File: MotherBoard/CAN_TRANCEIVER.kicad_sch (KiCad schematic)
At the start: 39 parts, among them U601 PTCAN1462DRQ1, U602 PTCAN1462DRQ1

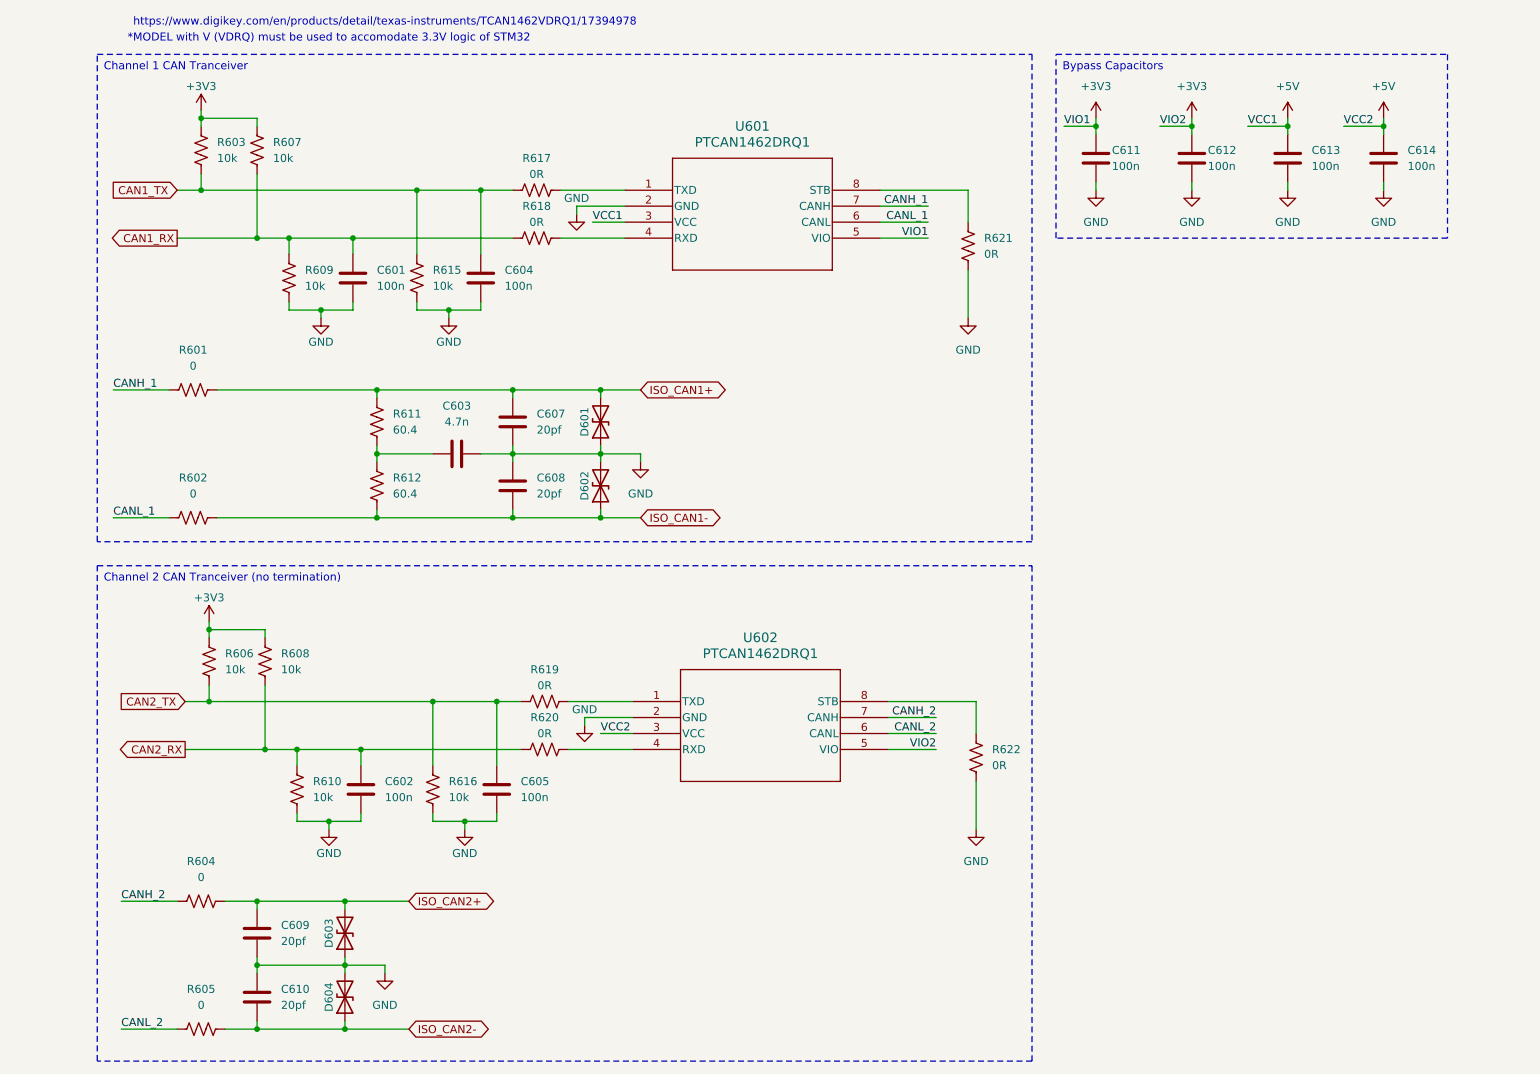
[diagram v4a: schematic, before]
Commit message: Added more 3D models
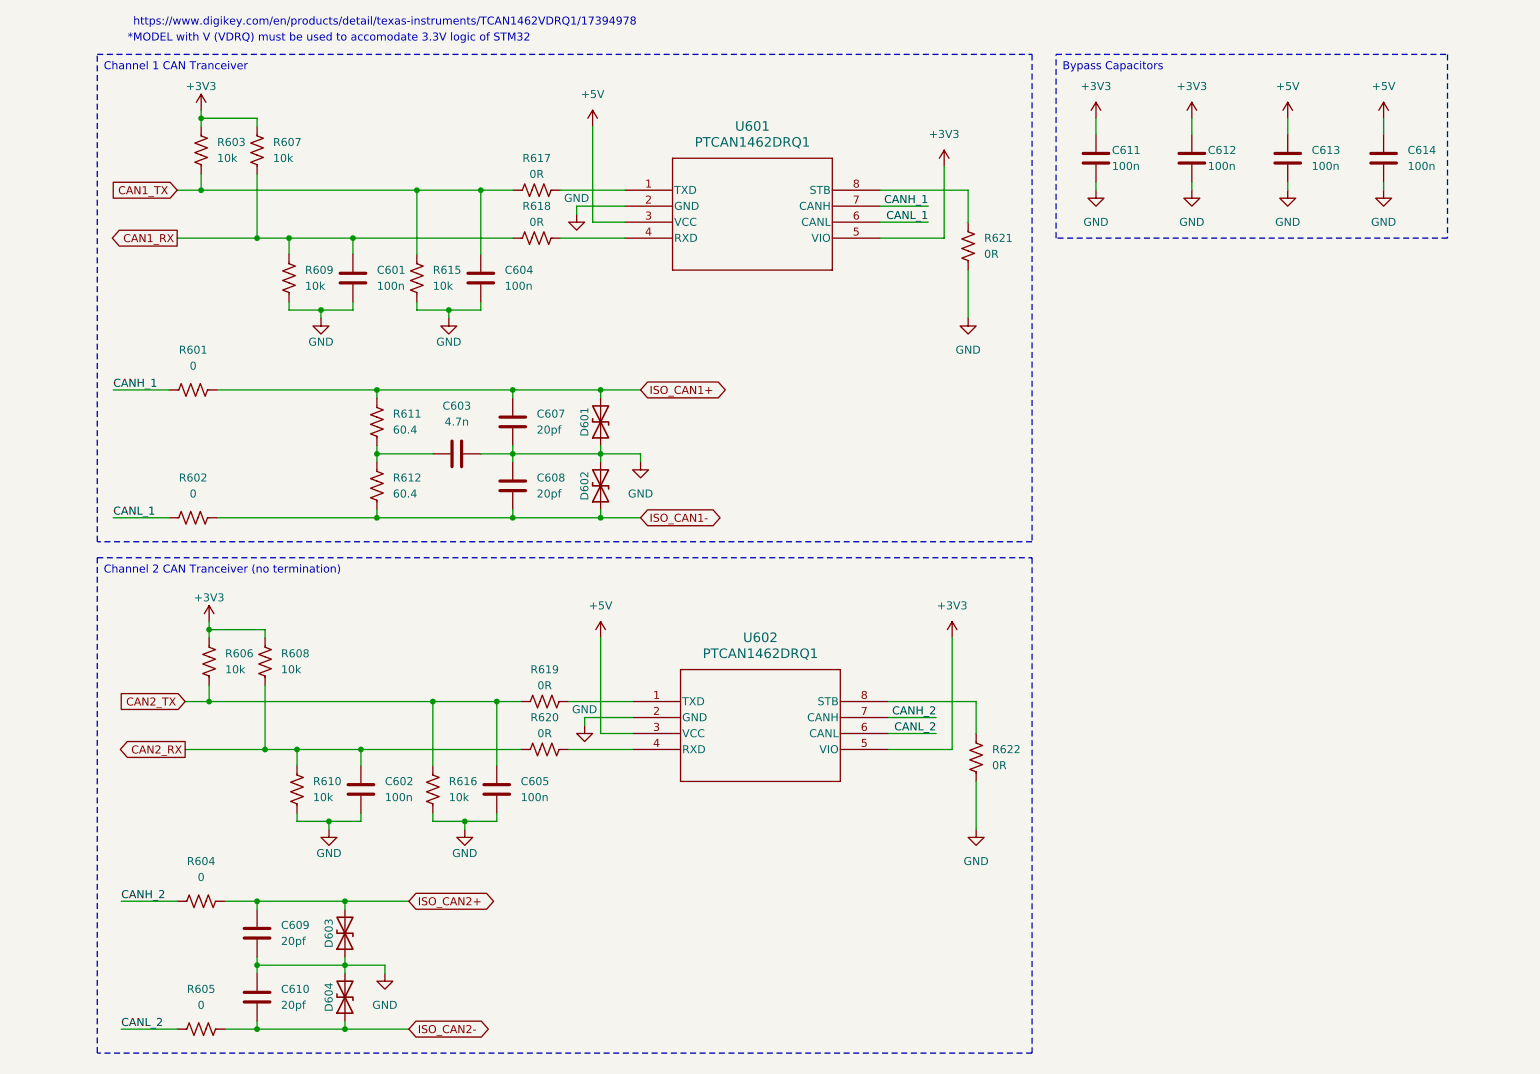
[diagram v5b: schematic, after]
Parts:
- C601, C602, C604, C605, C611, C612, C613, C614: footprint (none) -> Capacitor_SMD:C_0402_1005Metric
- R601, R602, R604, R605: footprint (none) -> Resistor_SMD:R_0402_1005Metric

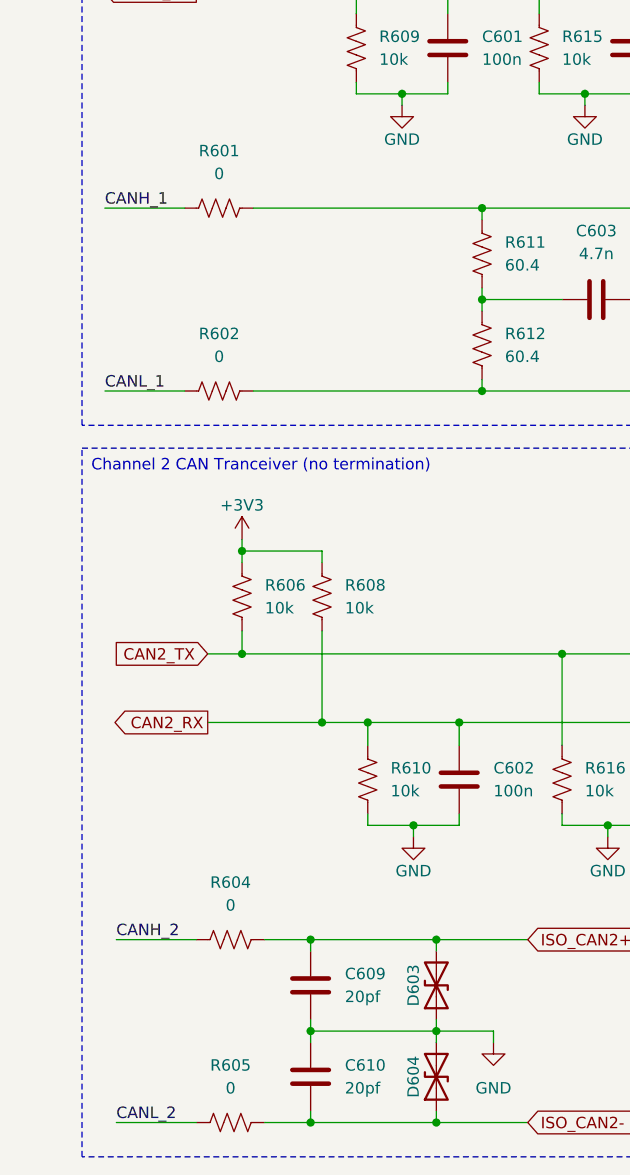
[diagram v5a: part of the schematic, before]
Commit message: Fixed relative paths + 90% footprints done + organized PCB for layout + found JLC part #s for manufacturing
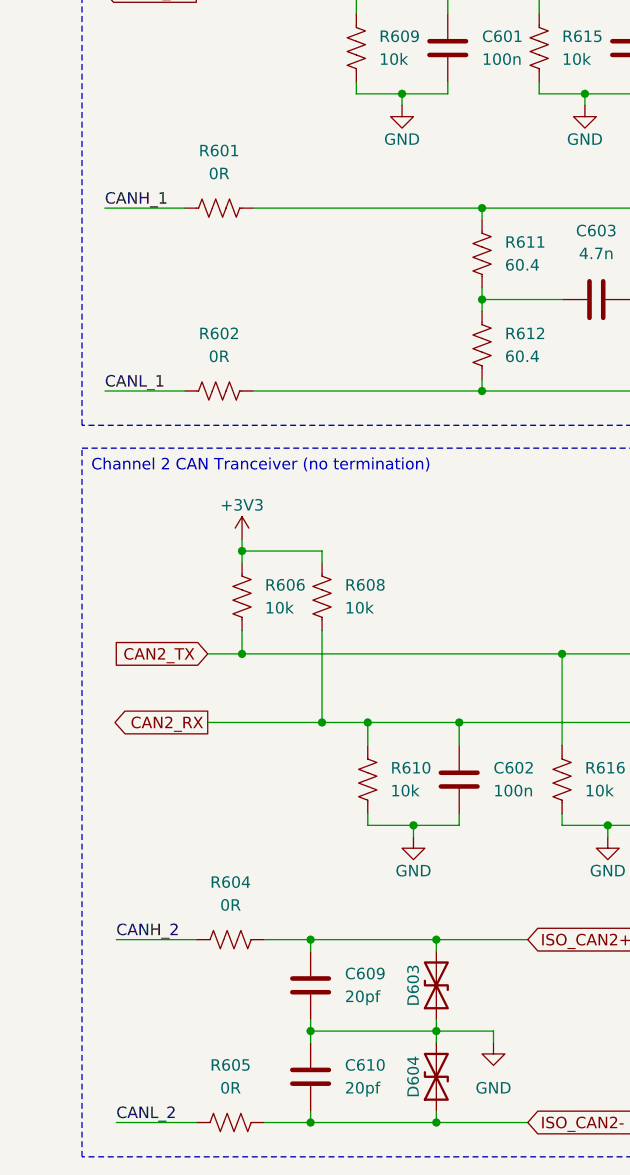
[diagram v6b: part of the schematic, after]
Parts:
- C603, C607, C608, C609, C610: footprint (none) -> Capacitor_SMD:C_0402_1005Metric
- R601, R602, R604, R605: value 0 -> 0R
- R603, R606, R607, R608, R609, R610, R615, R616, R617, R618, R619, R620, R621, R622: footprint (none) -> Resistor_SMD:R_0402_1005Metric
- U601, U602: Manufacturer_Part_Number (none) -> TCAN1462VDRQ1

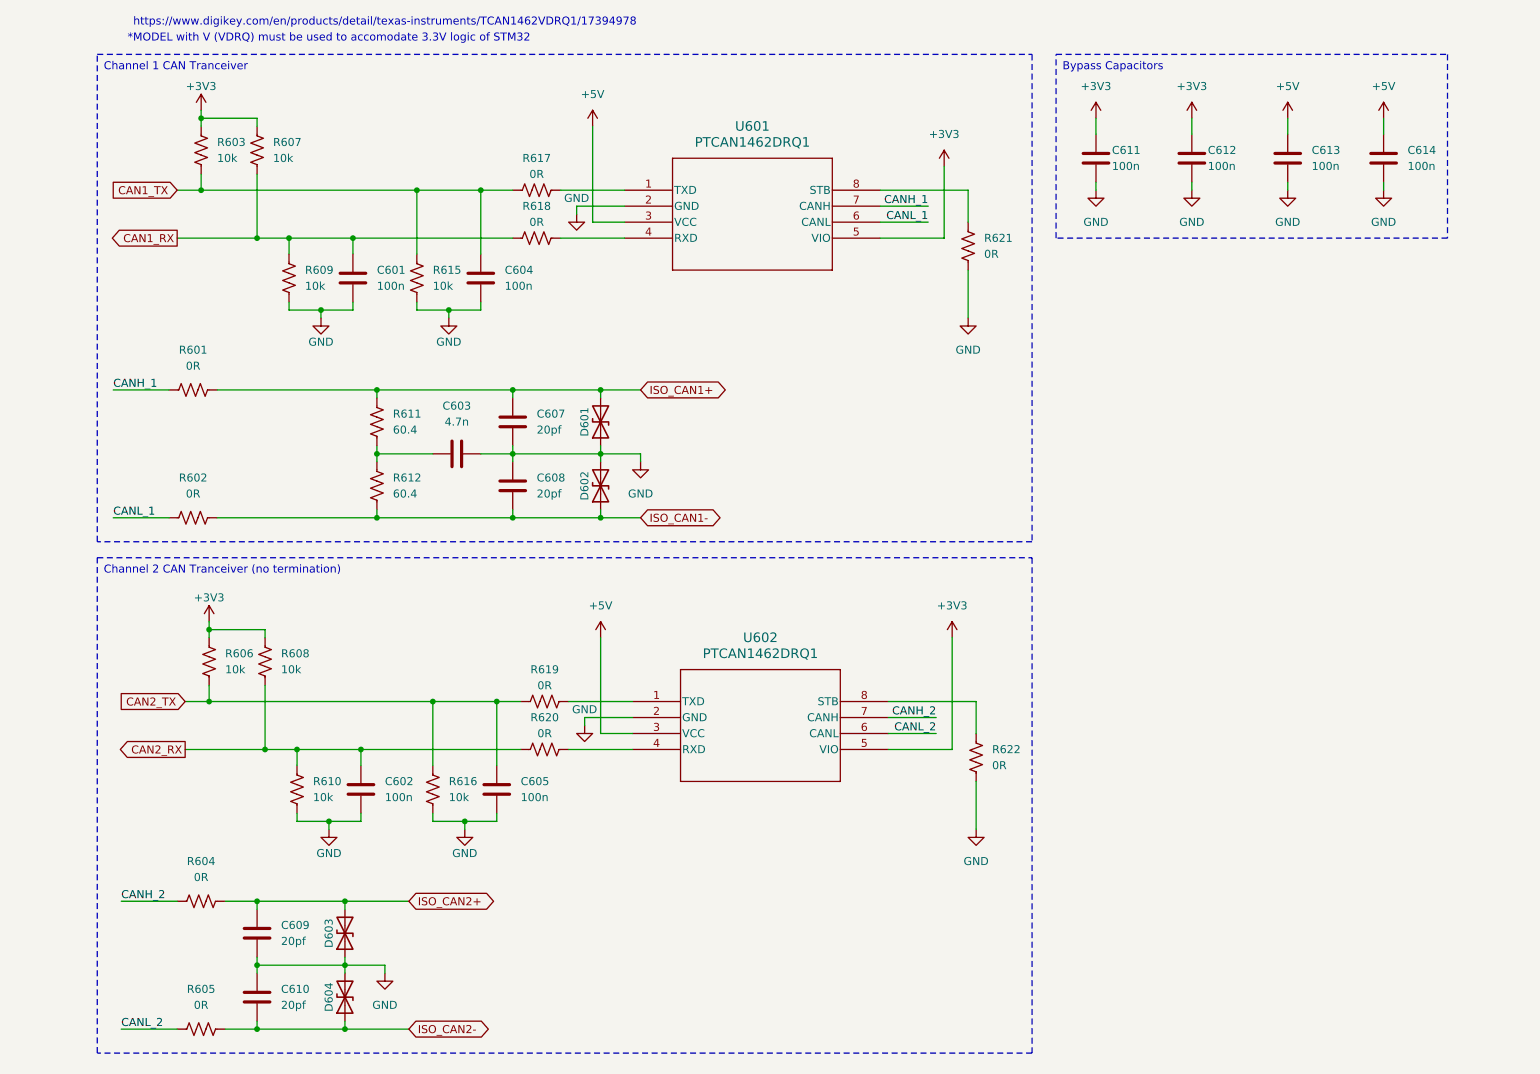
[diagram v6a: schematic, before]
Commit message: Completed BOM except inductors
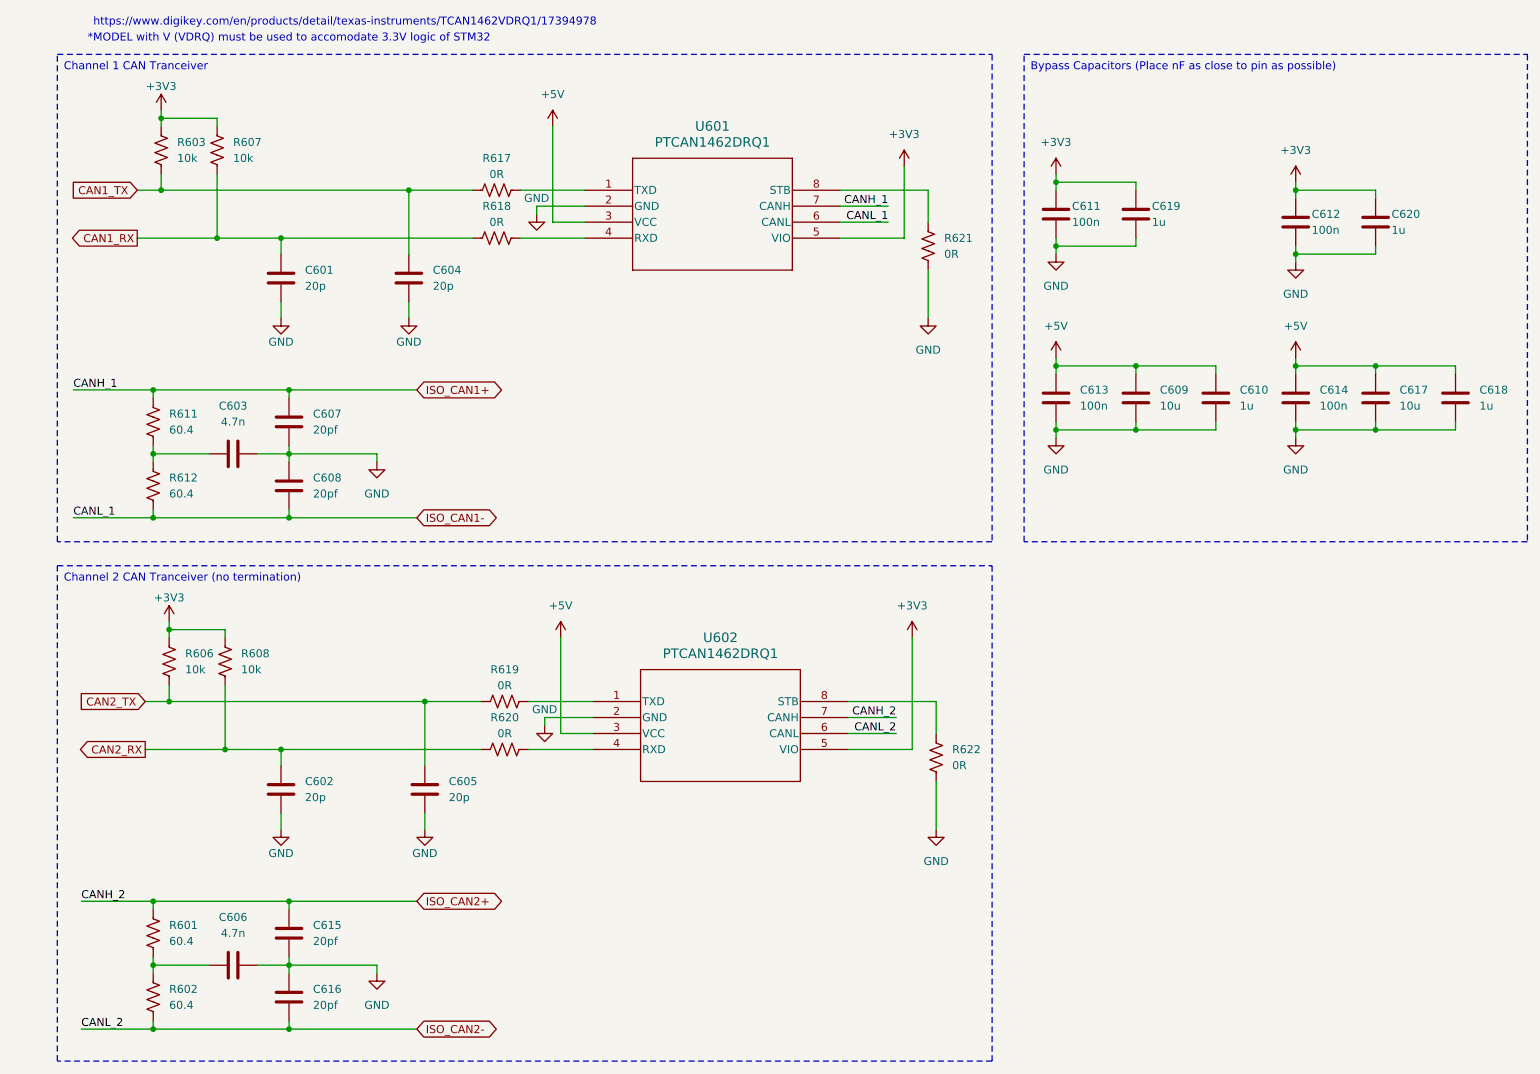
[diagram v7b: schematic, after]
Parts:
- removed D601, D602, D603, D604: D_TVS, Diode_SMD:D_SOD-323, symbol Device:D_TVS
- removed R604, R605: 0R, Resistor_SMD:R_0402_1005Metric, symbol Device:R_US
- removed R609, R610, R615, R616: 10k, Resistor_SMD:R_0402_1005Metric, symbol Device:R_US
- added C606: 4.7n, Capacitor_SMD:C_0402_1005Metric, symbol Device:C
- added C615, C616: 20pf, Capacitor_SMD:C_0402_1005Metric, symbol Device:C
- added C617: 10u, Capacitor_SMD:C_0603_1608Metric, symbol Device:C
- added C618, C619, C620: 1u, Capacitor_SMD:C_0402_1005Metric, symbol Device:C
- C601, C602, C604, C605: value 100n -> 20p; Manufacturer_Part_Number (none) -> 0402CG200J500NT
- C603: Manufacturer_Part_Number (none) -> CC0402JRX7R9BB472
- C607, C608: Manufacturer_Part_Number (none) -> 0402CG200J500NT
- C609: value 20pf -> 10u; footprint Capacitor_SMD:C_0402_1005Metric -> Capacitor_SMD:C_0603_1608Metric; Manufacturer_Part_Number (none) -> CL10A106KP8NNNC
- C610: value 20pf -> 1u; Manufacturer_Part_Number (none) -> CL05A105KO5NNNC
- C611, C612, C613, C614: Manufacturer_Part_Number (none) -> CL05B104KO5NNNC
- R601, R602: value 0R -> 60.4; footprint Resistor_SMD:R_0402_1005Metric -> Resistor_SMD:R_2512_6332Metric; Manufacturer_Part_Number (none) -> 25121WF604JT4E
- R603, R606, R607, R608: Manufacturer_Part_Number (none) -> 0402WGF1001TCE
- R611, R612: footprint (none) -> Resistor_SMD:R_2512_6332Metric; Manufacturer_Part_Number (none) -> 25121WF604JT4E
- R617, R618, R619, R620, R621, R622: footprint Resistor_SMD:R_0402_1005Metric -> Resistor_SMD:R_0805_2012Metric; Manufacturer_Part_Number (none) -> 0805W8F0000T5E
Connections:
- net CANH_2 is gone; now on net ISO_CAN2+: U602.7 (CANH)
- net CANL_2 is gone; now on net ISO_CAN2-: U602.6 (CANL)
- net +3V3: now also C619.1, C620.1
- net +5V: now also C609.1, C610.1, C617.1, C618.1
- net GND: now also C609.2, C606.2, C615.1, C616.2, C617.2, C618.2, C619.2, C620.2; no longer C609.1
- net ISO_CAN1+: now also U601.7 (CANH); no longer R601.1
- net ISO_CAN1-: now also U601.6 (CANL); no longer R602.1
- net ISO_CAN2+: now also R601.2, C615.2; no longer C609.2
- net ISO_CAN2-: now also R602.1, C616.1; no longer C610.1
- removed net CANH_1: R601.2, U601.7 (CANH)
- net CANL_1: no longer names the net of R602.2
- net CANL_1: now also R601.1, C606.1; no longer U601.6 (CANL)
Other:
- moved on the sheet: C601, C602, C603, C604, C605, C607, C608, C611, C612, C613, R603, R606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
